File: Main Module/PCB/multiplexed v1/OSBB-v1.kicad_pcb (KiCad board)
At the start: 2 copper layers, 21 parts, among them P1 AUX 1-3, P14 EXTRA Pins, P2 Wire to Teensy VUSB, P3 +3.3V, P4 Pit limiter, P5 Rotary Encoders, P6 BTN 1-32, Q1 Q_NPN_CBE, Q2 Q_NPN_CBE, Q3 Q_NPN_CBE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

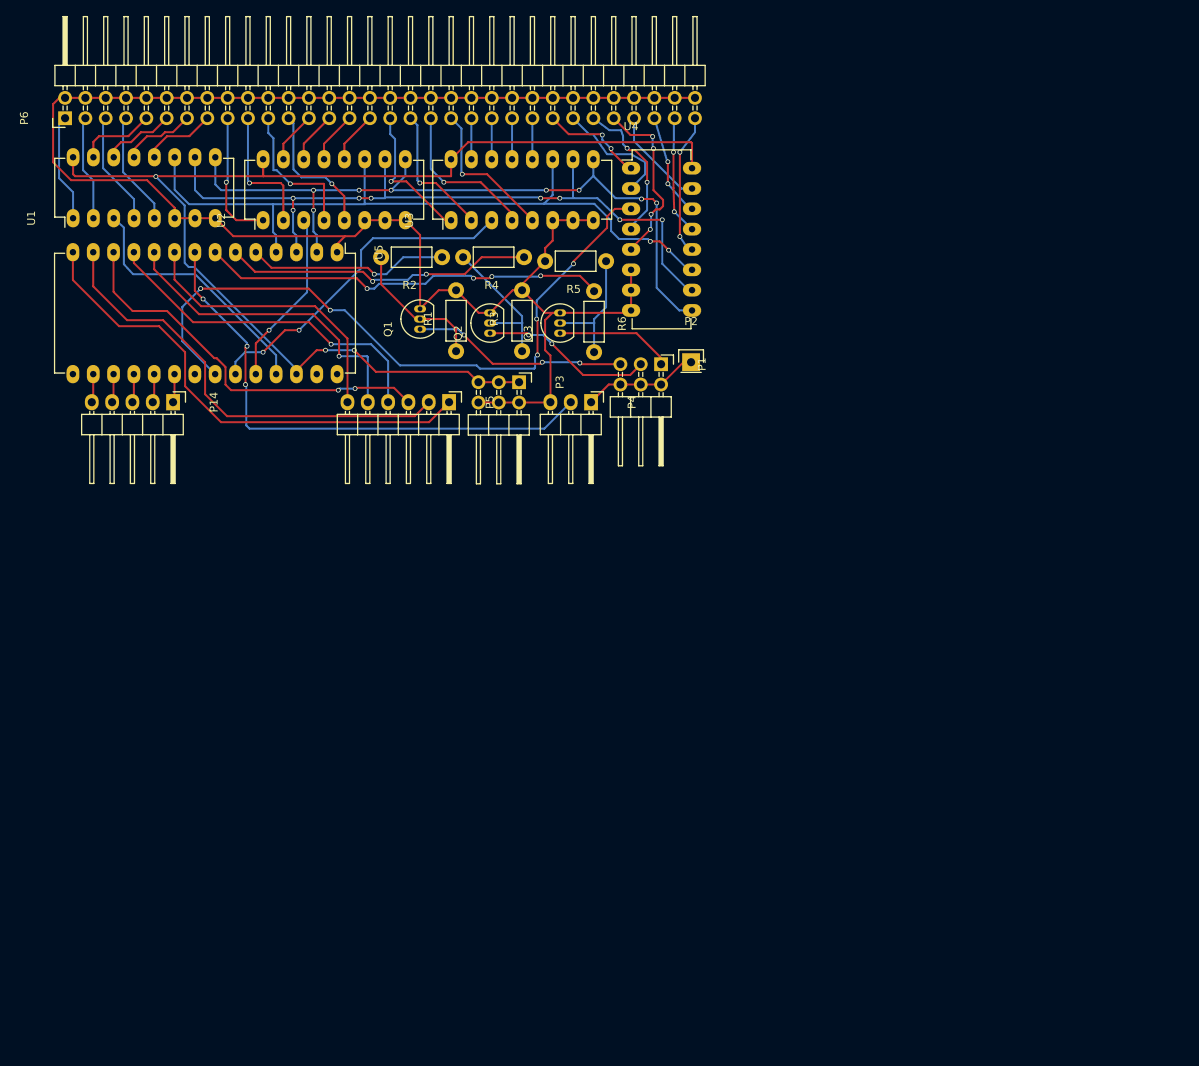
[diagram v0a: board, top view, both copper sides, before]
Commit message: * added perimiter to PCB layout
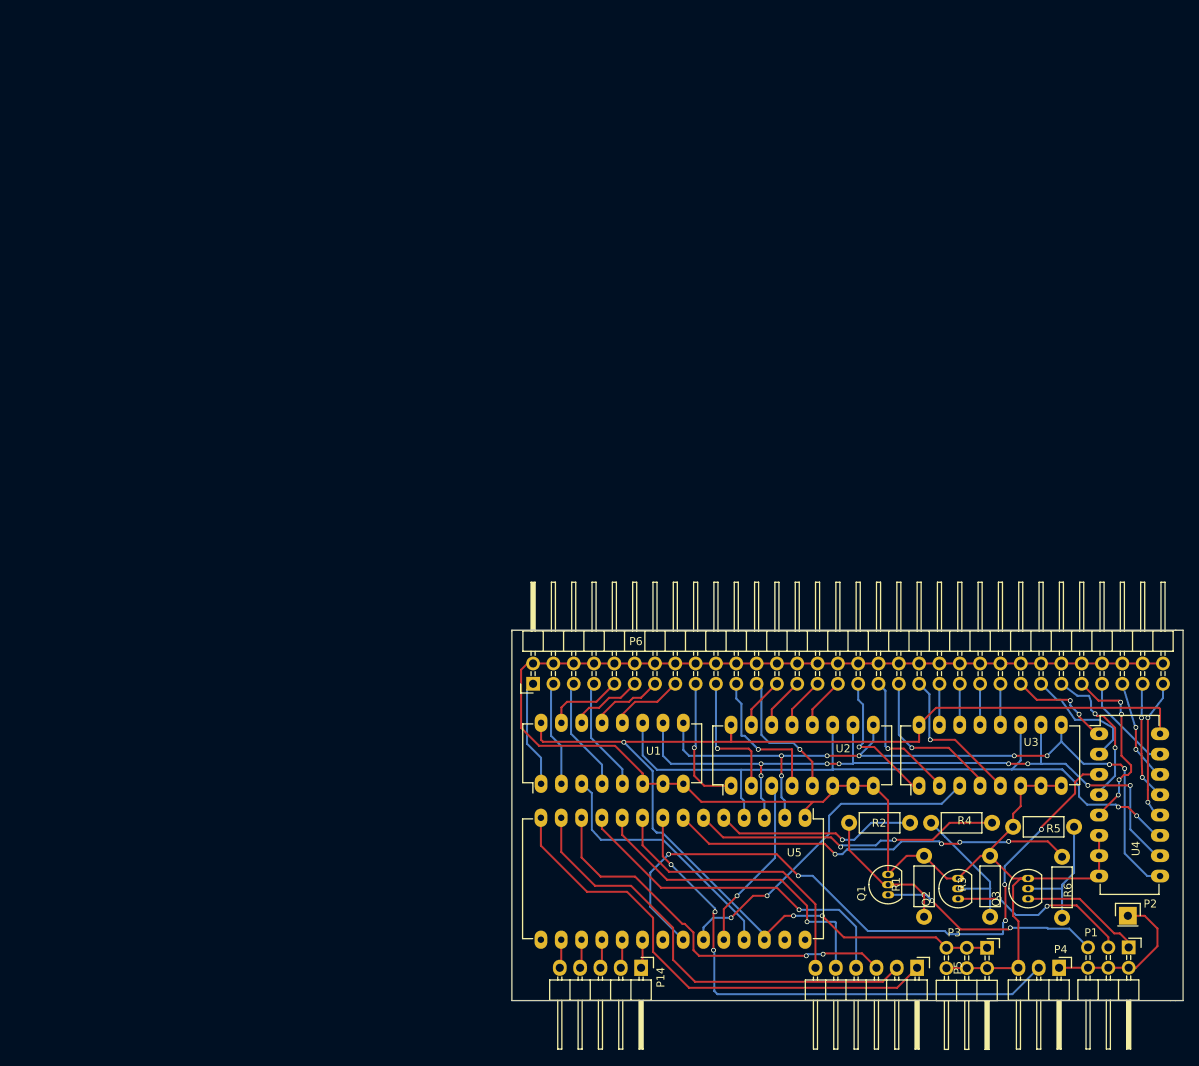
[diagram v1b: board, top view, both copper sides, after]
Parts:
- P2: value Wire to Teensy VUSB -> VUSB
- moved P1 93.4 mm to (247.2, 126.7)
- moved P14 91.8 mm to (186.2, 129.2)
- moved P3 91.8 mm to (229.5, 126.7)
- moved P4 91.8 mm to (238.5, 129.2)
- moved P5 91.8 mm to (220.8, 129.2)
- moved P6 91.8 mm to (172.8, 93.7)
- moved Q1 91.8 mm to (217.1, 120.1)
- moved Q2 91.8 mm to (225.9, 120.6)
- moved Q3 91.8 mm to (234.6, 120.6)
- moved R1 91.8 mm to (221.6, 122.8)
- moved R2 91.8 mm to (219.9, 111.1)
- moved R3 91.8 mm to (229.9, 122.8)
- moved R4 91.8 mm to (230.1, 111.1)
- moved R5 91.8 mm to (240.4, 111.6)
- moved R6 91.8 mm to (238.9, 115.3)
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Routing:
- net +5V: track 14.6 -> 20.0 mm
- net Net-(P1-Pad3): track 21.6 -> 23.1 mm
- net Net-(P1-Pad5): track 27.0 -> 27.9 mm, vias 3 -> 2
- net Net-(P1-Pad1): track 14.7 -> 15.5 mm
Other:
- board outline added: 83.9 x 46.3 mm
- net class Thicker added: clearance 0.2, trace_width 0.5, via_dia 0.7, via_drill 0.5

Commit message: * tweaked a few traces
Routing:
- net Net-(U2-Pad3): track 22.1 -> 23.2 mm
- net Net-(U1-Pad10): track 91.3 -> 91.9 mm
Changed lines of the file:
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@@
     (links 137)
     (no_connects 0)
-    (area 108.175 9.574999 200.533335 69.425001)
+    (area 170.049999 80.274999 254.050001 140.125001)
     (thickness 1.6)
     (drawings 8)
-    (tracks 617)
+    (tracks 624)
     (zones 0)
     (modules 21)
@@
   (segment (start 203.8 102.7) (end 209.5 102.7) (width 0.25) (layer B.Cu) (net 21))
   (segment (start 191.53 101.98) (end 192.25 102.7) (width 0.25) (layer B.Cu) (net 21))
+  (segment (start 201.25 107.95) (end 201.25 105.15) (width 0.25) (layer B.Cu) (net 22))
+  (segment (start 201.67 110.45) (end 201.67 108.37) (width 0.25) (layer B.Cu) (net 22))
+  (segment (start 201.67 108.37) (end 201.25 107.95) (width 0.25) (layer B.Cu) (net 22))
+  (segment (start 201.3 103.7) (end 201.9 103.7) (width 0.25) (layer B.Cu) (net 22))
+  (via (at 201.3 103.7) (size 0.6) (drill 0.4) (layers F.Cu B.Cu) (net 22))
+  (segment (start 201.3 105.1) (end 201.3 103.7) (width 0.25) (layer F.Cu) (net 22))
+  (via (at 201.3 105.1) (size 0.6) (drill 0.4) (layers F.Cu B.Cu) (net 22))
+  (segment (start 201.25 105.15) (end 201.3 105.1) (width 0.25) (layer B.Cu) (net 22))
   (segment (start 251.12 115.19) (end 250.69 115.19) (width 0.25) (layer B.Cu) (net 22))
   (segment (start 250.69 115.19) (end 247.4 111.9) (width 0.25) (layer B.Cu) (net 22))
@@
   (via (at 232.2 103.7) (size 0.6) (drill 0.4) (layers F.Cu B.Cu) (net 22))
   (segment (start 232.1 103.6) (end 232.2 103.7) (width 0.25) (layer B.Cu) (net 22))
-  (segment (start 201.67 110.45) (end 201.67 108.37) (width 0.25) (layer B.Cu) (net 22))
-  (via (at 201.25 103.7) (size 0.6) (drill 0.4) (layers F.Cu B.Cu) (net 22))
-  (segment (start 201.25 105.2) (end 201.25 103.7) (width 0.25) (layer F.Cu) (net 22))
-  (via (at 201.25 105.2) (size 0.6) (drill 0.4) (layers F.Cu B.Cu) (net 22))
-  (segment (start 201.25 107.95) (end 201.25 105.2) (width 0.25) (layer B.Cu) (net 22))
-  (segment (start 201.67 108.37) (end 201.25 107.95) (width 0.25) (layer B.Cu) (net 22))
   (segment (start 188.99 98.58) (end 188.99 102.69) (width 0.25) (layer B.Cu) (net 22))
   (segment (start 212.74 103.69) (end 212.74 103.6) (width 0.25) (layer B.Cu) (net 22))
@@
   (via (at 209.5 103.7) (size 0.6) (drill 0.4) (layers F.Cu B.Cu) (net 22))
   (segment (start 190 103.7) (end 201.25 103.7) (width 0.25) (layer B.Cu) (net 22))
-  (segment (start 201.25 103.7) (end 209.5 103.7) (width 0.25) (layer B.Cu) (net 22))
+  (segment (start 201.25 103.7) (end 201.9 103.7) (width 0.25) (layer B.Cu) (net 22))
+  (segment (start 201.9 103.7) (end 209.5 103.7) (width 0.25) (layer B.Cu) (net 22))
   (segment (start 188.99 102.69) (end 190 103.7) (width 0.25) (layer B.Cu) (net 22))
   (segment (start 251.12 112.65) (end 250.65 112.65) (width 0.25) (layer B.Cu) (net 23))
@@
   (segment (start 238.75 95.7) (end 238.25 95.7) (width 0.25) (layer B.Cu) (net 57))
   (segment (start 238.25 95.7) (end 236.25 93.7) (width 0.25) (layer B.Cu) (net 57))
+  (segment (start 242.5 95.95) (end 241.04 95.95) (width 0.25) (layer B.Cu) (net 58))
+  (segment (start 242.5 96.95) (end 242.5 95.95) (width 0.25) (layer B.Cu) (net 58))
+  (segment (start 243 97.45) (end 242.5 96.95) (width 0.25) (layer B.Cu) (net 58))
+  (via (at 243 97.45) (size 0.6) (drill 0.4) (layers F.Cu B.Cu) (net 58))
+  (segment (start 243.25 97.7) (end 243 97.45) (width 0.25) (layer F.Cu) (net 58))
+  (segment (start 244 97.7) (end 243.25 97.7) (width 0.25) (layer F.Cu) (net 58))
+  (segment (start 245.5 99.2) (end 244 97.7) (width 0.25) (layer F.Cu) (net 58))
+  (segment (start 245.5 101.7) (end 245.5 99.2) (width 0.25) (layer F.Cu) (net 58))
+  (via (at 245.5 101.7) (size 0.6) (drill 0.4) (layers F.Cu B.Cu) (net 58))
+  (segment (start 245.5 105.2) (end 245.5 101.7) (width 0.25) (layer B.Cu) (net 58))
+  (segment (start 243.5 107.2) (end 245.5 105.2) (width 0.25) (layer B.Cu) (net 58))
+  (segment (start 241.04 95.95) (end 238.79 93.7) (width 0.25) (layer B.Cu) (net 58))
   (segment (start 243.5 107.57) (end 243.5 107.2) (width 0.25) (layer B.Cu) (net 58))
-  (segment (start 243.5 107.2) (end 245.5 105.2) (width 0.25) (layer B.Cu) (net 58))
-  (segment (start 245.5 105.2) (end 245.5 101.7) (width 0.25) (layer B.Cu) (net 58))
-  (via (at 245.5 101.7) (size 0.6) (drill 0.4) (layers F.Cu B.Cu) (net 58))
-  (segment (start 245.5 101.7) (end 245.5 99.2) (width 0.25) (layer F.Cu) (net 58))
-  (segment (start 245.5 99.2) (end 244 97.7) (width 0.25) (layer F.Cu) (net 58))
-  (segment (start 244 97.7) (end 243.25 97.7) (width 0.25) (layer F.Cu) (net 58))
-  (segment (start 243.25 97.7) (end 243 97.45) (width 0.25) (layer F.Cu) (net 58))
-  (via (at 243 97.45) (size 0.6) (drill 0.4) (layers F.Cu B.Cu) (net 58))
-  (segment (start 243 97.45) (end 242.5 96.95) (width 0.25) (layer B.Cu) (net 58))
-  (segment (start 242.5 96.95) (end 242.5 95.95) (width 0.25) (layer B.Cu) (net 58))
-  (segment (start 242.5 95.95) (end 242.25 95.2) (width 0.25) (layer B.Cu) (net 58))
-  (segment (start 242.25 95.2) (end 240.79 95.2) (width 0.25) (layer B.Cu) (net 58))
-  (segment (start 240.79 95.2) (end 238.79 93.7) (width 0.25) (layer B.Cu) (net 58))
   (segment (start 243.5 110.11) (end 243.5 110) (width 0.25) (layer F.Cu) (net 59))
   (segment (start 243.5 110) (end 245.9 107.6) (width 0.25) (layer F.Cu) (net 59))
@@
   (segment (start 189 113.2) (end 181.25 113.2) (width 0.25) (layer B.Cu) (net 64))
   (segment (start 199.13 123.33) (end 189 113.2) (width 0.25) (layer B.Cu) (net 64))
-  (segment (start 196.59 125.69) (end 196.59 121.86) (width 0.25) (layer F.Cu) (net 65))
-  (segment (start 203 115.45) (end 203 106.87) (width 0.25) (layer B.Cu) (net 65))
+  (segment (start 202.58 106.45) (end 202.58 108.78) (width 0.25) (layer B.Cu) (net 65) (status 400000))
+  (segment (start 196.59 121.86) (end 196.59 125.69) (width 0.25) (layer F.Cu) (net 65))
   (segment (start 198.25 120.2) (end 203 115.45) (width 0.25) (layer B.Cu) (net 65))
   (via (at 198.25 120.2) (size 0.6) (drill 0.4) (layers F.Cu B.Cu) (net 65))
   (segment (start 196.59 121.86) (end 198.25 120.2) (width 0.25) (layer F.Cu) (net 65))
+  (segment (start 203.7 114.75) (end 203 115.45) (width 0.25) (layer B.Cu) (net 65))
+  (segment (start 203.7 112.5) (end 203.7 114.75) (width 0.25) (layer B.Cu) (net 65))
+  (segment (start 202.9 111.7) (end 203.7 112.5) (width 0.25) (layer B.Cu) (net 65))
+  (segment (start 202.9 109.1) (end 202.9 111.7) (width 0.25) (layer B.Cu) (net 65))
+  (segment (start 202.58 108.78) (end 202.9 109.1) (width 0.25) (layer B.Cu) (net 65))
   (segment (start 203 106.87) (end 202.58 106.45) (width 0.25) (layer B.Cu) (net 65))
   (segment (start 194.05 125.69) (end 194.05 124.15) (width 0.25) (layer B.Cu) (net 66))

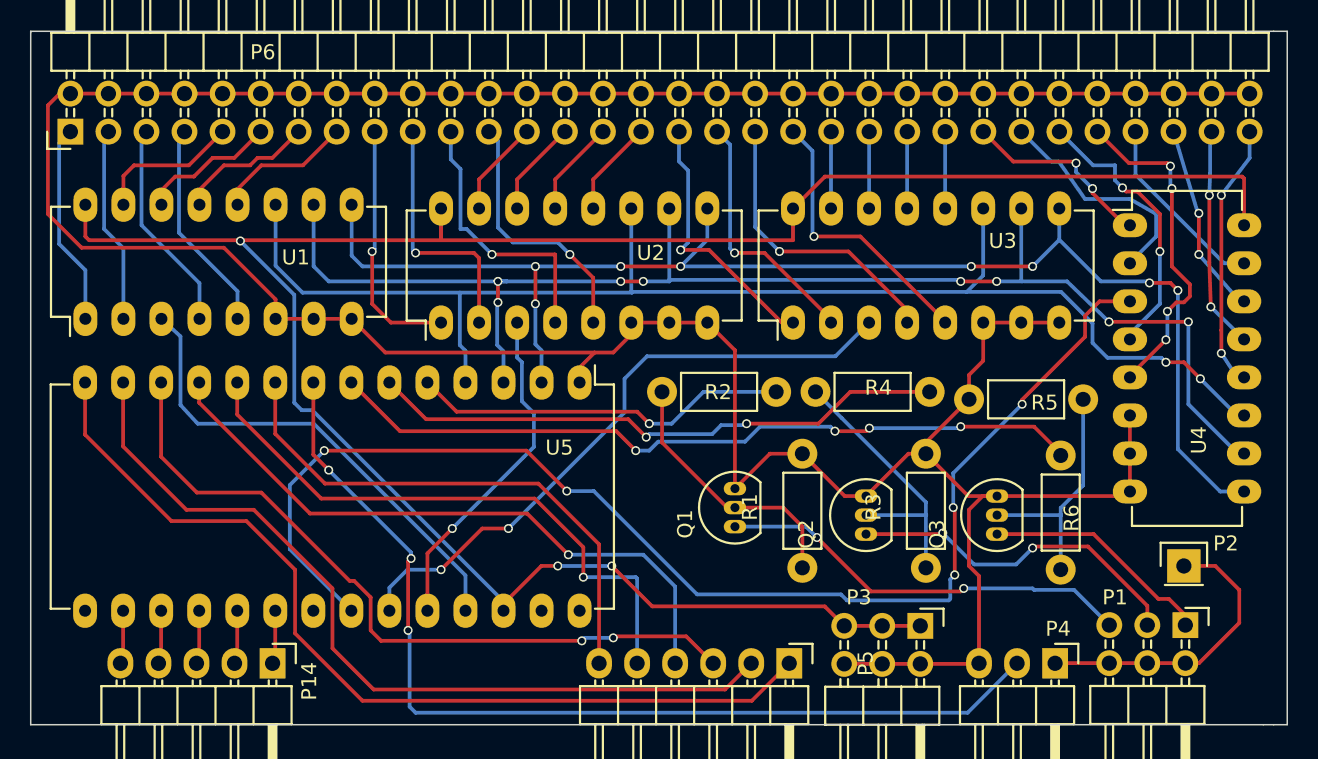
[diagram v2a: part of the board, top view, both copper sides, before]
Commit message: * GND traces thicker from 0.25mm to 0.5mm * +5V traces thicker from 0.25mm to 0.75mm
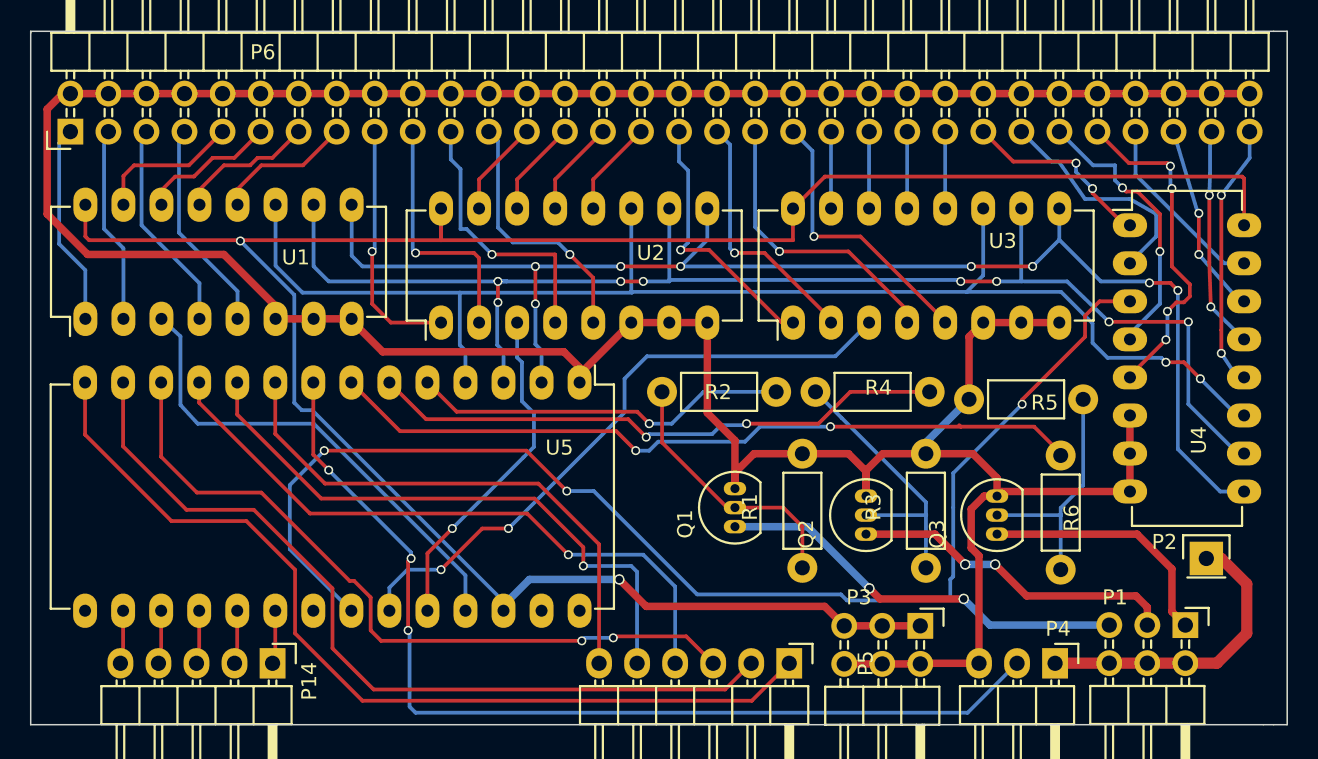
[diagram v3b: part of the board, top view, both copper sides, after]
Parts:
- moved P2 1.58 mm to (248.6, 122.2)
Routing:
- net GND: track 225.3 -> 230.8 mm
- net Net-(P1-Pad1): track 15.5 -> 17.4 mm
- net Net-(P1-Pad3): track 23.1 -> 22.0 mm
- net +3V3: track 155.7 -> 155.3 mm, vias 3 -> 2
- net Net-(R6-Pad1): track 51.0 -> 50.9 mm, vias 4 -> 2
- net Net-(U4-Pad3): vias 5 -> 3
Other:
- net class 5Volt added: clearance 0.4, trace_width 0.75, via_dia 0.6, via_drill 0.4

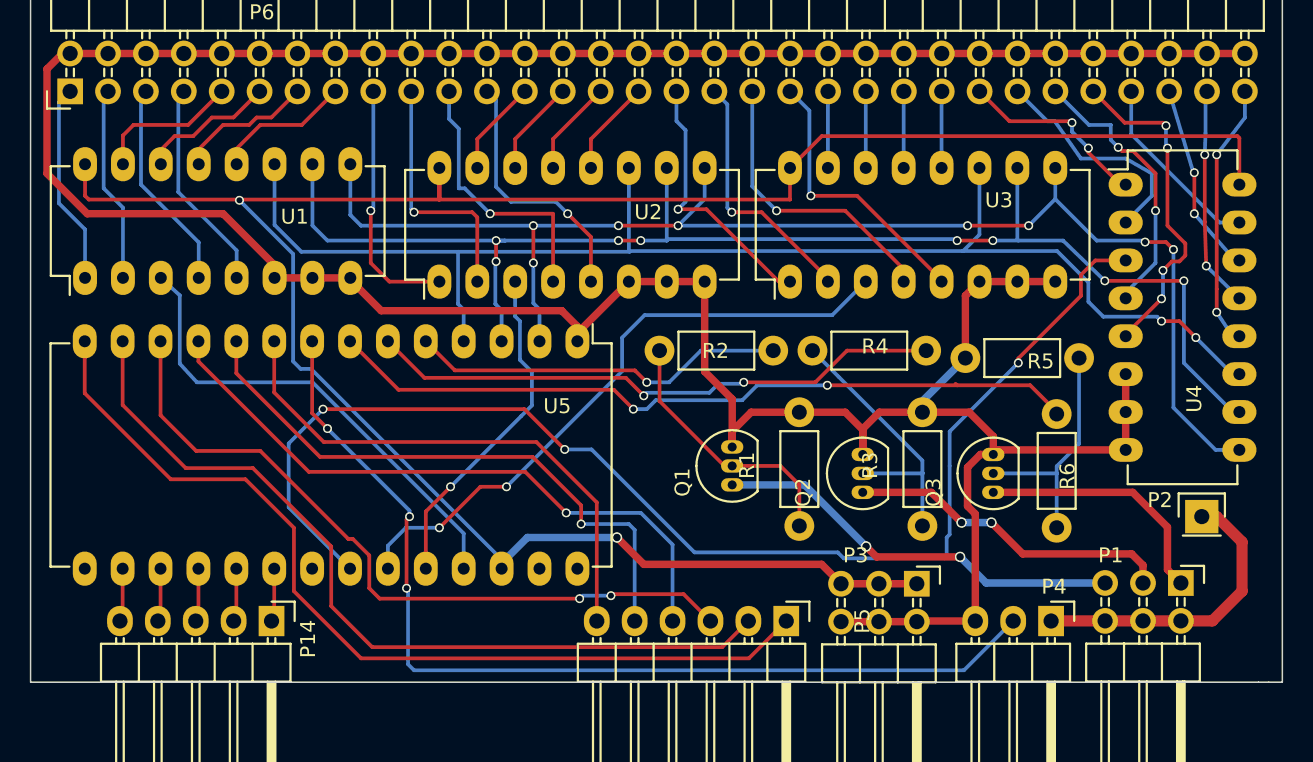
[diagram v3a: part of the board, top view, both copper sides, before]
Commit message: * tweaked layout of a few traces * added two M2 mounting holes
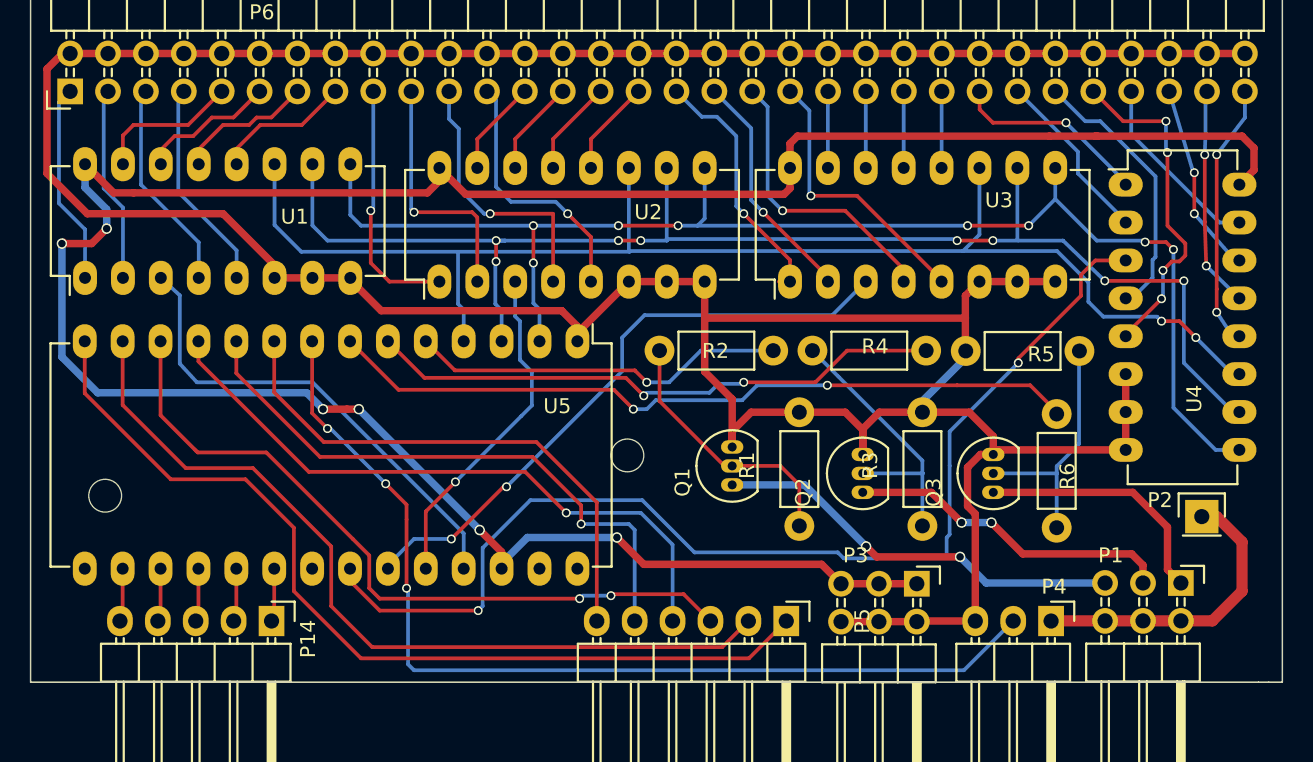
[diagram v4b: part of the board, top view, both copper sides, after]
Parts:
- added REF**: M2, Mounting_Holes:MountingHole_2.2mm_M2, F.Cu at (210.1, 118.1)
- added REF**: M2, Mounting_Holes:MountingHole_2.2mm_M2, F.Cu at (175.1, 120.8)
- moved R5 0.48 mm to (240.4, 111.1)
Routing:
- net GND: track 230.8 -> 248.0 mm
- net +3V3: track 155.3 -> 171.1 mm, vias 2 -> 6
- net Net-(U4-Pad3): track 85.4 -> 74.7 mm, vias 3 -> 2
- net Net-(P6-Pad51): track 15.4 -> 11.8 mm
- net Net-(P6-Pad35): track 17.1 -> 16.1 mm
- net Net-(U3-Pad3): track 42.2 -> 41.5 mm
- net Net-(P6-Pad33): track 17.9 -> 17.2 mm
- net Net-(P6-Pad49): track 12.9 -> 13.5 mm, vias 2 -> 1
- net Net-(U1-Pad9): track 92.0 -> 91.5 mm
- net Net-(P6-Pad53): track 18.8 -> 18.7 mm, vias 2 -> 0
